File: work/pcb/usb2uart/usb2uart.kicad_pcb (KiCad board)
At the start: 2 copper layers, 32 x 18 mm, 13 parts, among them J1 USB, J2 HEADER, U1 CP2104

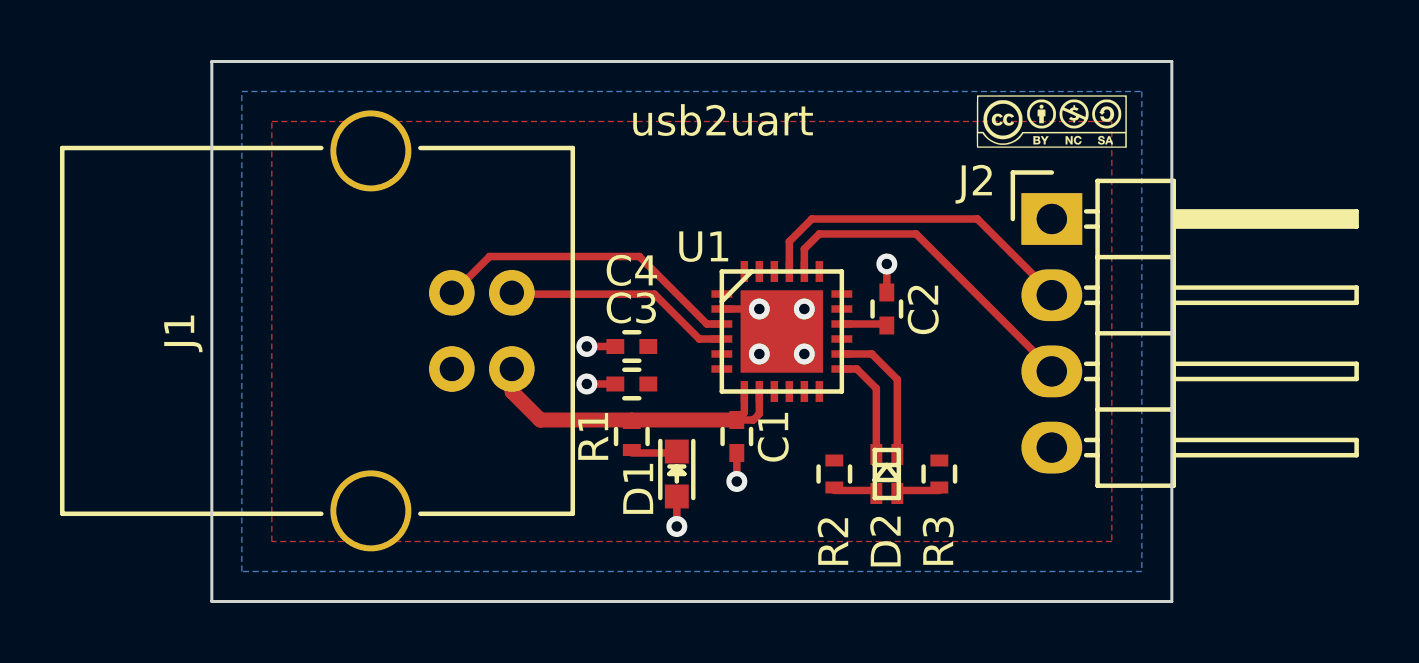
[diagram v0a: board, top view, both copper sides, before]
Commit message: [pcb] πρώτη ολοκληρωμένη έκδοση κυκλώματος, μαζί με αρχεία παραγωγής
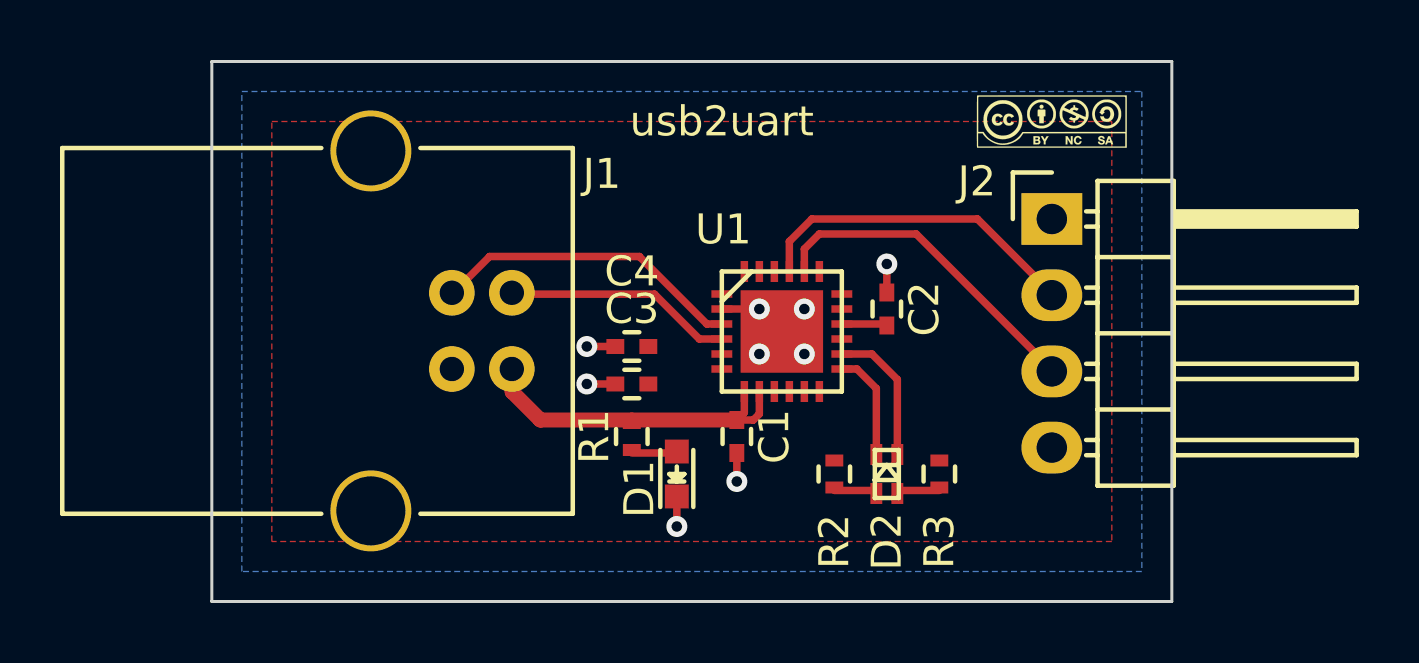
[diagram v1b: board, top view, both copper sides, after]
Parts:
- turned D1 to 90 degrees
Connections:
- D1 pad 1: /LEDONR -> GND
- D1 pad 2: GND -> /LEDONR
- U1 pad 1: (no net) -> Net-(U1-Pad1)
- U1 pad 10: (no net) -> Net-(U1-Pad10)
- U1 pad 11: (no net) -> Net-(U1-Pad11)
- U1 pad 12: (no net) -> Net-(U1-Pad12)
- U1 pad 15: (no net) -> Net-(U1-Pad15)
- U1 pad 17: (no net) -> Net-(U1-Pad17)
- U1 pad 18: (no net) -> Net-(U1-Pad18)
- U1 pad 19: (no net) -> Net-(U1-Pad19)
- U1 pad 22: (no net) -> Net-(U1-Pad22)
- U1 pad 23: (no net) -> Net-(U1-Pad23)
- U1 pad 24: (no net) -> Net-(U1-Pad24)
